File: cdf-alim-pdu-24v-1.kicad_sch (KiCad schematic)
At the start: 133 parts, among them J1 Conn_01x02, J10 Conn_01x02, J11 Conn_01x02, J12 Conn_01x02, J13 Conn_01x02, J14 Conn_01x02, J15 Conn_01x02, J16 Conn_01x02, J17 Conn_01x02, J18 Conn_01x02, J19 Conn_01x02, J3 Conn_01x02, J5 Conn_01x02, J6 Conn_01x02, J7 Conn_01x02, J8 Conn_01x02, J9 Conn_01x02, Q3 BSC019N04LS, Q4 BSC019N04LS, Q5 BSC019N04LS, U1 HT753-1, U2 TPS25983, U3 TPS25983, U4 TPS25983, U5 MX25947, U6 MX25947, U7 MX25947

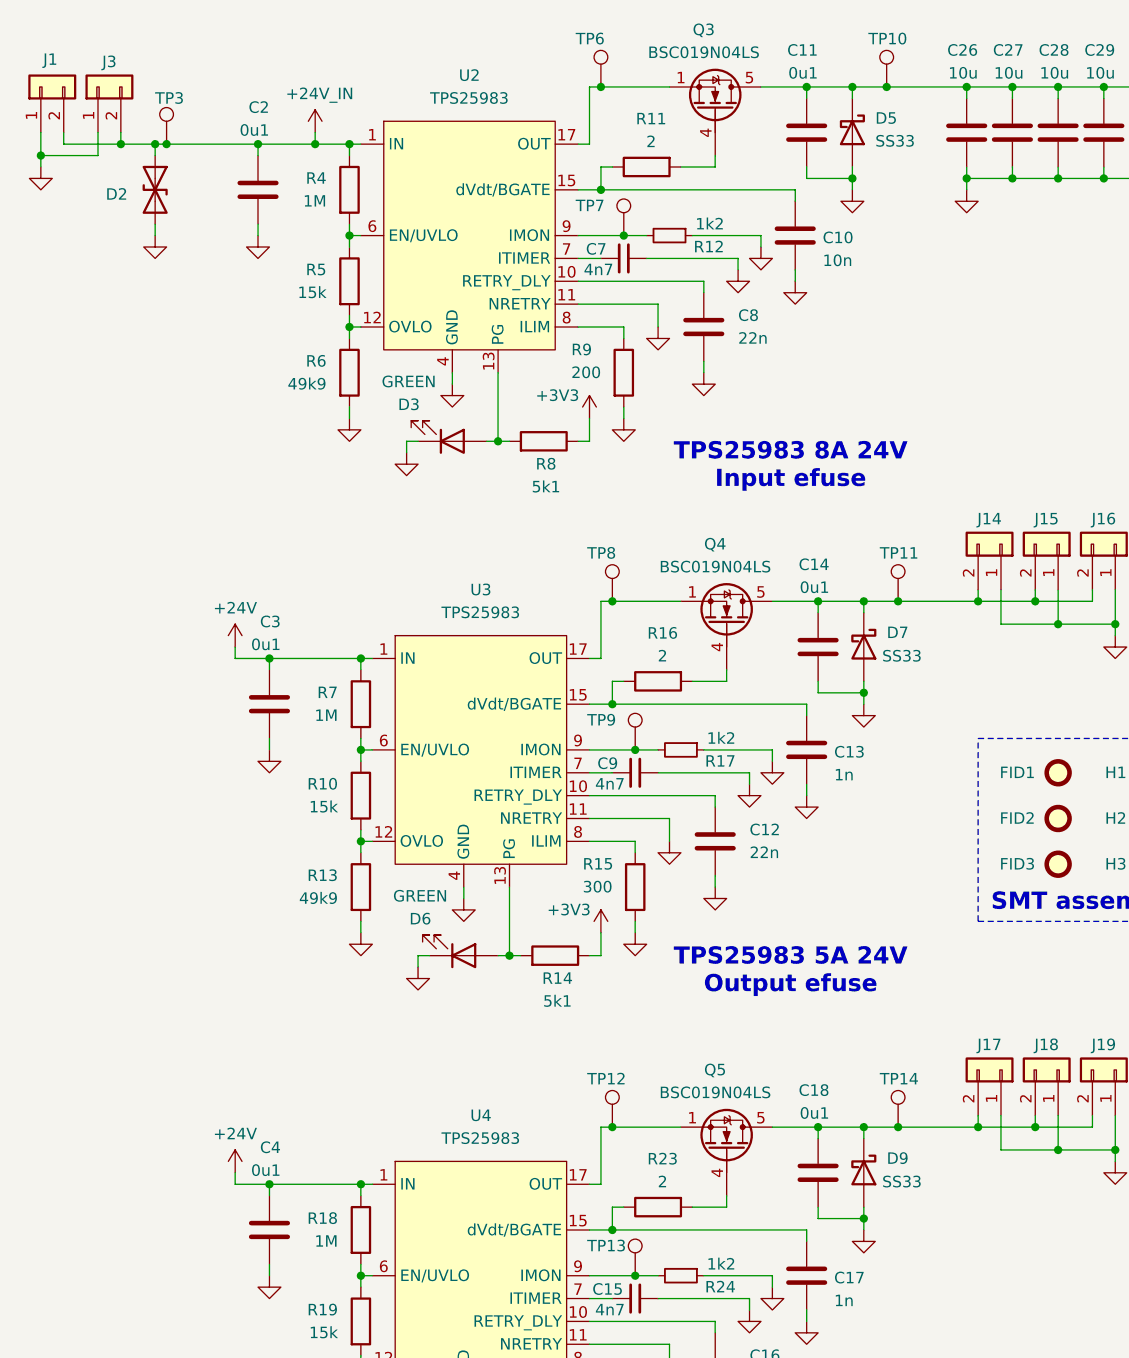
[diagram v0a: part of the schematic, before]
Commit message: schem: run and fix DRC
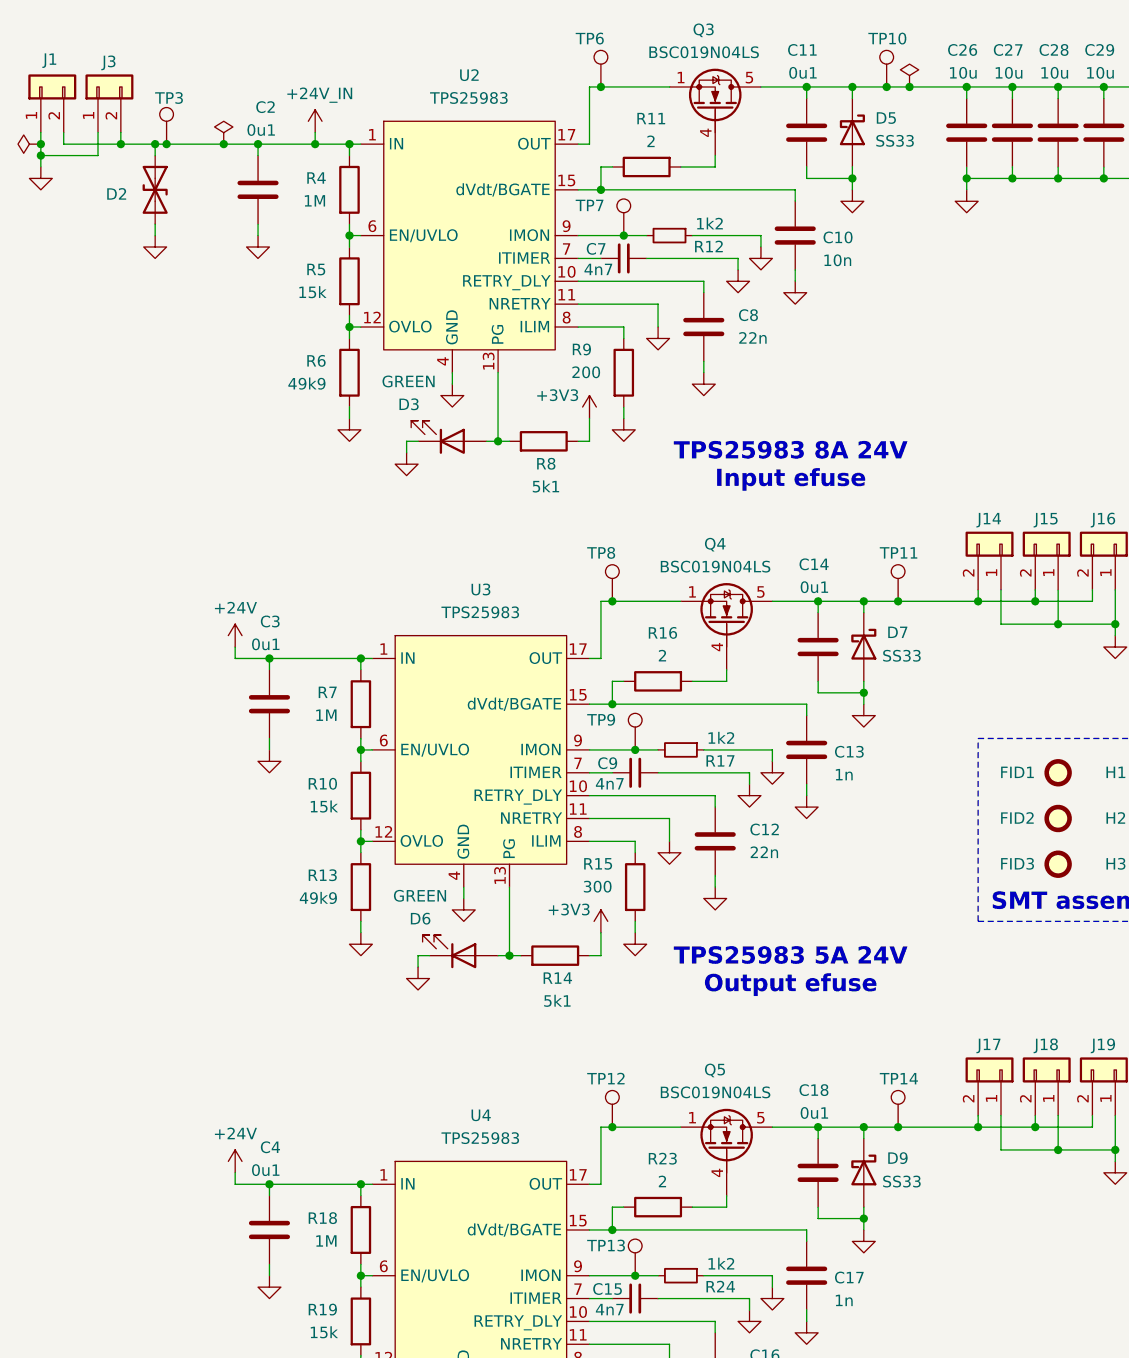
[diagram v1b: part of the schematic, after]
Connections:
- net +24V: no longer C2.1, D2.1 (A1), J1.2 (Pin_2), J3.2 (Pin_2), R4.1, TP3.1, U2.1 (IN), U2.16 (IN), U2.2 (IN), U2.25 (IN), U2.3 (IN)
- new net +24V_IN: C2.1, D2.1 (A1), J1.2 (Pin_2), J3.2 (Pin_2), R4.1, TP3.1, U2.1 (IN), U2.16 (IN), U2.2 (IN), U2.25 (IN), U2.3 (IN)
